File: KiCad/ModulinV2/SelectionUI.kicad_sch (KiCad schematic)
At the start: 24 parts, among them IC44 E-ULN2003D1013TR, IC45 E-ULN2003D1013TR, IC46 CD4028BM96, IC47 CD4028BM96

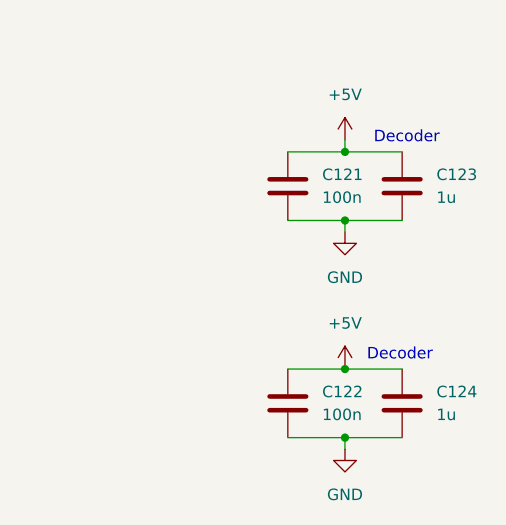
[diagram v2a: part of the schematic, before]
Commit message: Added footprints to all capacitors and potentiometers
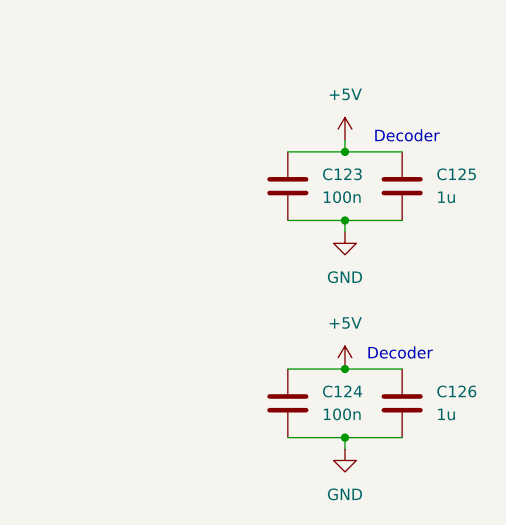
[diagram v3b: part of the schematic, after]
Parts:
- C123: renamed from C121; footprint SamacSys_Parts:CAPC1608X90N -> Capacitor_SMD:C_0603_1608Metric_Pad1.08x0.95mm_HandSolder
- C124: renamed from C122; footprint SamacSys_Parts:CAPC1608X90N -> Capacitor_SMD:C_0603_1608Metric_Pad1.08x0.95mm_HandSolder
- C125: renamed from C123; footprint SamacSys_Parts:CAPC1608X95N -> Capacitor_SMD:C_0603_1608Metric_Pad1.08x0.95mm_HandSolder
- C126: renamed from C124; footprint SamacSys_Parts:CAPC1608X95N -> Capacitor_SMD:C_0603_1608Metric_Pad1.08x0.95mm_HandSolder
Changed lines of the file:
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@@
 		(dnp no)
 		(fields_autoplaced yes)
-		(property "Reference" "#PWR0299"
+		(property "Reference" "#PWR0301"
 			(at 265.43 163.83 0)
 			(effects
@@
 			(project "ModulinV2"
 				(path "/c6b34a57-3941-4b56-8b80-1848c7f41082/ba5ade70-a939-4914-9429-1ad400c74d73/e799dfb0-018d-4a0c-90e3-bc5a892eb818"
-					(reference "#PWR0299")
+					(reference "#PWR0301")
 					(unit 1)
 				)
@@
 		(dnp no)
 		(fields_autoplaced yes)
-		(property "Reference" "#PWR0290"
+		(property "Reference" "#PWR0292"
 			(at 140.97 88.9 0)
 			(effects
@@
 			(project "ModulinV2"
 				(path "/c6b34a57-3941-4b56-8b80-1848c7f41082/ba5ade70-a939-4914-9429-1ad400c74d73/e799dfb0-018d-4a0c-90e3-bc5a892eb818"
-					(reference "#PWR0290")
+					(reference "#PWR0292")
 					(unit 1)
 				)
@@
 		(dnp no)
 		(fields_autoplaced yes)
-		(property "Reference" "#PWR0292"
+		(property "Reference" "#PWR0294"
 			(at 198.12 97.79 0)
 			(effects
@@
 			(project "ModulinV2"
 				(path "/c6b34a57-3941-4b56-8b80-1848c7f41082/ba5ade70-a939-4914-9429-1ad400c74d73/e799dfb0-018d-4a0c-90e3-bc5a892eb818"
-					(reference "#PWR0292")
+					(reference "#PWR0294")
 					(unit 1)
 				)
@@
 		(dnp no)
 		(fields_autoplaced yes)
-		(property "Reference" "#PWR0289"
+		(property "Reference" "#PWR0291"
 			(at 140.97 50.8 0)
 			(effects
@@
 			(project ""
 				(path "/c6b34a57-3941-4b56-8b80-1848c7f41082/ba5ade70-a939-4914-9429-1ad400c74d73/e799dfb0-018d-4a0c-90e3-bc5a892eb818"
-					(reference "#PWR0289")
+					(reference "#PWR0291")
 					(unit 1)
 				)
@@
 		(dnp no)
 		(fields_autoplaced yes)
-		(property "Reference" "#PWR0287"
+		(property "Reference" "#PWR0289"
 			(at 17.78 26.67 0)
 			(effects
@@
 			(project ""
 				(path "/c6b34a57-3941-4b56-8b80-1848c7f41082/ba5ade70-a939-4914-9429-1ad400c74d73/e799dfb0-018d-4a0c-90e3-bc5a892eb818"
-					(reference "#PWR0287")
+					(reference "#PWR0289")
 					(unit 1)
 				)
@@
 		(dnp no)
 		(fields_autoplaced yes)
-		(property "Reference" "#PWR0288"
+		(property "Reference" "#PWR0290"
 			(at 17.78 95.25 0)
 			(effects
@@
 			(project "ModulinV2"
 				(path "/c6b34a57-3941-4b56-8b80-1848c7f41082/ba5ade70-a939-4914-9429-1ad400c74d73/e799dfb0-018d-4a0c-90e3-bc5a892eb818"
-					(reference "#PWR0288")
+					(reference "#PWR0290")
 					(unit 1)
 				)
@@
 		(dnp no)
 		(fields_autoplaced yes)
-		(property "Reference" "#PWR0291"
+		(property "Reference" "#PWR0293"
 			(at 198.12 53.34 0)
 			(effects
@@
 			(project "ModulinV2"
 				(path "/c6b34a57-3941-4b56-8b80-1848c7f41082/ba5ade70-a939-4914-9429-1ad400c74d73/e799dfb0-018d-4a0c-90e3-bc5a892eb818"
-					(reference "#PWR0291")
+					(reference "#PWR0293")
 					(unit 1)
 				)
@@
 		(dnp no)
 		(fields_autoplaced yes)
-		(property "Reference" "C121"
+		(property "Reference" "C123"
 			(at 262.89 126.9999 0)
 			(effects
@@
 			)
 		)
-		(property "Footprint" "SamacSys_Parts:CAPC1608X90N"
+		(property "Footprint" "Capacitor_SMD:C_0603_1608Metric_Pad1.08x0.95mm_HandSolder"
 			(at 258.1148 124.46 0)
 			(effects
@@
 			(project "ModulinV2"
 				(path "/c6b34a57-3941-4b56-8b80-1848c7f41082/ba5ade70-a939-4914-9429-1ad400c74d73/e799dfb0-018d-4a0c-90e3-bc5a892eb818"
-					(reference "C121")
+					(reference "C123")
 					(unit 1)
 				)
@@
 		(dnp no)
 		(fields_autoplaced yes)
-		(property "Reference" "#PWR0296"
+		(property "Reference" "#PWR0298"
 			(at 265.43 127 0)
 			(effects
@@
 			(project "ModulinV2"
 				(path "/c6b34a57-3941-4b56-8b80-1848c7f41082/ba5ade70-a939-4914-9429-1ad400c74d73/e799dfb0-018d-4a0c-90e3-bc5a892eb818"
-					(reference "#PWR0296")
+					(reference "#PWR0298")
 					(unit 1)
 				)
@@
 		(dnp no)
 		(fields_autoplaced yes)
-		(property "Reference" "C123"
+		(property "Reference" "C125"
 			(at 275.59 126.9999 0)
 			(effects
@@
 			)
 		)
-		(property "Footprint" "SamacSys_Parts:CAPC1608X95N"
+		(property "Footprint" "Capacitor_SMD:C_0603_1608Metric_Pad1.08x0.95mm_HandSolder"
 			(at 270.8148 124.46 0)
 			(effects
@@
 			(project "ModulinV2"
 				(path "/c6b34a57-3941-4b56-8b80-1848c7f41082/ba5ade70-a939-4914-9429-1ad400c74d73/e799dfb0-018d-4a0c-90e3-bc5a892eb818"
-					(reference "C123")
+					(reference "C125")
 					(unit 1)
 				)
@@
 		(dnp no)
 		(fields_autoplaced yes)
-		(property "Reference" "#PWR0294"
+		(property "Reference" "#PWR0296"
 			(at 223.52 72.39 0)
 			(effects
@@
 			(project "ModulinV2"
 				(path "/c6b34a57-3941-4b56-8b80-1848c7f41082/ba5ade70-a939-4914-9429-1ad400c74d73/e799dfb0-018d-4a0c-90e3-bc5a892eb818"
-					(reference "#PWR0294")
+					(reference "#PWR0296")
 					(unit 1)
 				)
@@
 		(dnp no)
 		(fields_autoplaced yes)
-		(property "Reference" "#PWR0293"
+		(property "Reference" "#PWR0295"
 			(at 223.52 27.94 0)
 			(effects
@@
 			(project "ModulinV2"
 				(path "/c6b34a57-3941-4b56-8b80-1848c7f41082/ba5ade70-a939-4914-9429-1ad400c74d73/e799dfb0-018d-4a0c-90e3-bc5a892eb818"
-					(reference "#PWR0293")
+					(reference "#PWR0295")
 					(unit 1)
 				)
@@
 		(dnp no)
 		(fields_autoplaced yes)
-		(property "Reference" "C122"
+		(property "Reference" "C124"
 			(at 262.89 151.1299 0)
 			(effects
@@
 			)
 		)
-		(property "Footprint" "SamacSys_Parts:CAPC1608X90N"
+		(property "Footprint" "Capacitor_SMD:C_0603_1608Metric_Pad1.08x0.95mm_HandSolder"
 			(at 258.1148 148.59 0)
 			(effects
@@
 			(project "ModulinV2"
 				(path "/c6b34a57-3941-4b56-8b80-1848c7f41082/ba5ade70-a939-4914-9429-1ad400c74d73/e799dfb0-018d-4a0c-90e3-bc5a892eb818"
-					(reference "C122")
+					(reference "C124")
 					(unit 1)
 				)
@@
 		(dnp no)
 		(fields_autoplaced yes)
-		(property "Reference" "#PWR0295"
+		(property "Reference" "#PWR0297"
 			(at 233.68 90.17 0)
 			(effects
@@
 			(project "ModulinV2"
 				(path "/c6b34a57-3941-4b56-8b80-1848c7f41082/ba5ade70-a939-4914-9429-1ad400c74d73/e799dfb0-018d-4a0c-90e3-bc5a892eb818"
-					(reference "#PWR0295")
+					(reference "#PWR0297")
 					(unit 1)
 				)
@@
 		(dnp no)
 		(fields_autoplaced yes)
-		(property "Reference" "#PWR0297"
+		(property "Reference" "#PWR0299"
 			(at 265.43 139.7 0)
 			(effects
@@
 			(project "ModulinV2"
 				(path "/c6b34a57-3941-4b56-8b80-1848c7f41082/ba5ade70-a939-4914-9429-1ad400c74d73/e799dfb0-018d-4a0c-90e3-bc5a892eb818"
-					(reference "#PWR0297")
+					(reference "#PWR0299")
 					(unit 1)
 				)
@@
 		(dnp no)
 		(fields_autoplaced yes)
-		(property "Reference" "#PWR0298"
+		(property "Reference" "#PWR0300"
 			(at 265.43 152.4 0)
 			(effects
@@
 			(project "ModulinV2"
 				(path "/c6b34a57-3941-4b56-8b80-1848c7f41082/ba5ade70-a939-4914-9429-1ad400c74d73/e799dfb0-018d-4a0c-90e3-bc5a892eb818"
-					(reference "#PWR0298")
+					(reference "#PWR0300")
 					(unit 1)
 				)
@@
 		(dnp no)
 		(fields_autoplaced yes)
-		(property "Reference" "C124"
+		(property "Reference" "C126"
 			(at 275.59 151.1299 0)
 			(effects
@@
 			)
 		)
-		(property "Footprint" "SamacSys_Parts:CAPC1608X95N"
+		(property "Footprint" "Capacitor_SMD:C_0603_1608Metric_Pad1.08x0.95mm_HandSolder"
 			(at 270.8148 148.59 0)
 			(effects
@@
 			(project "ModulinV2"
 				(path "/c6b34a57-3941-4b56-8b80-1848c7f41082/ba5ade70-a939-4914-9429-1ad400c74d73/e799dfb0-018d-4a0c-90e3-bc5a892eb818"
-					(reference "C124")
+					(reference "C126")
 					(unit 1)
 				)

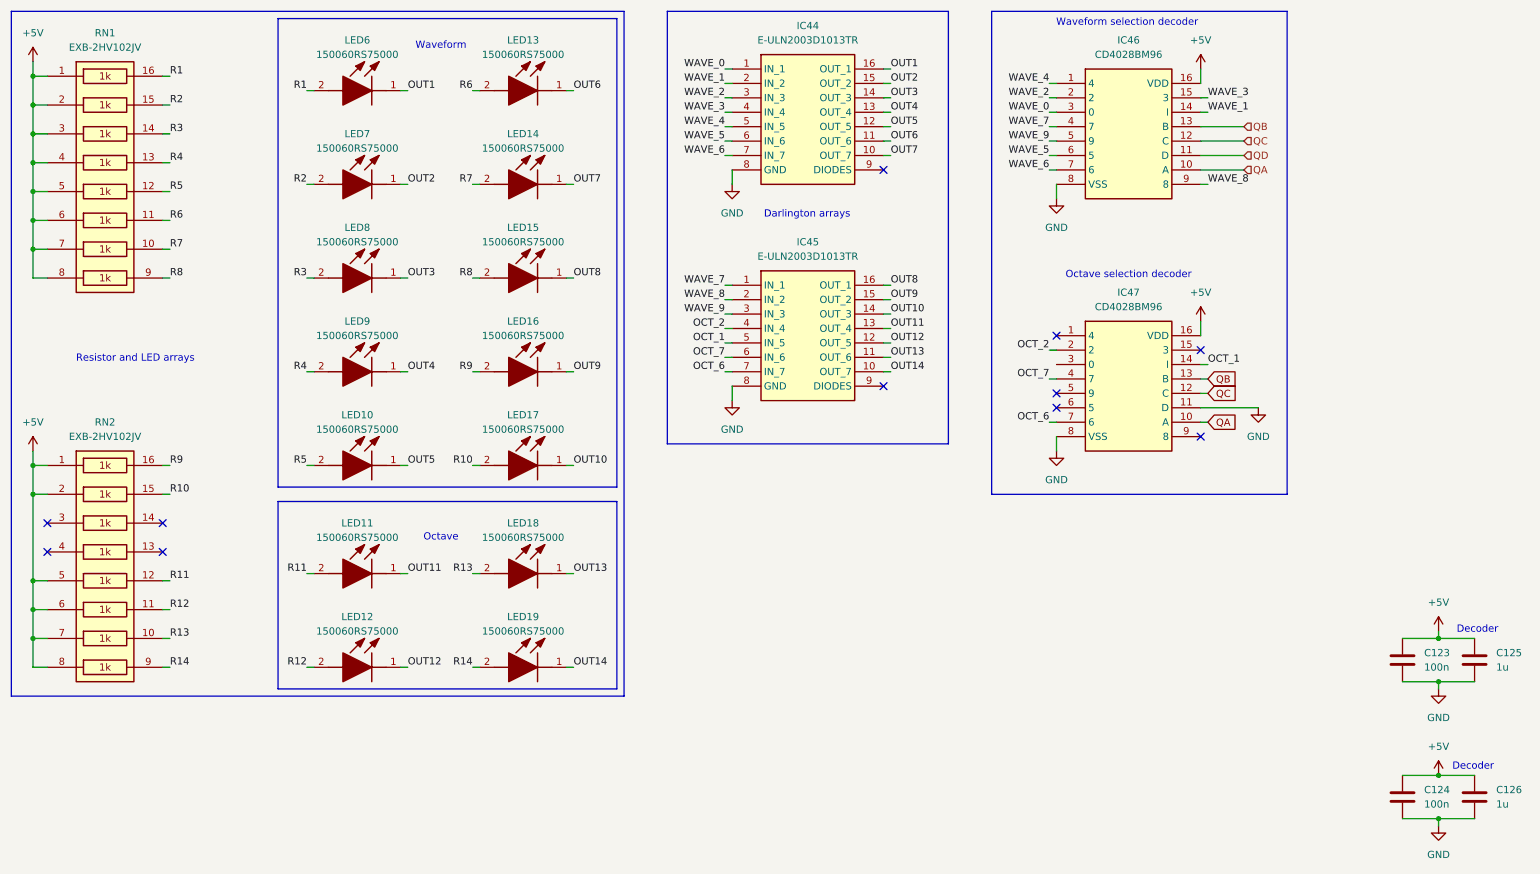
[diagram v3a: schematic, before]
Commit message: Finished Schematic, started on PCB
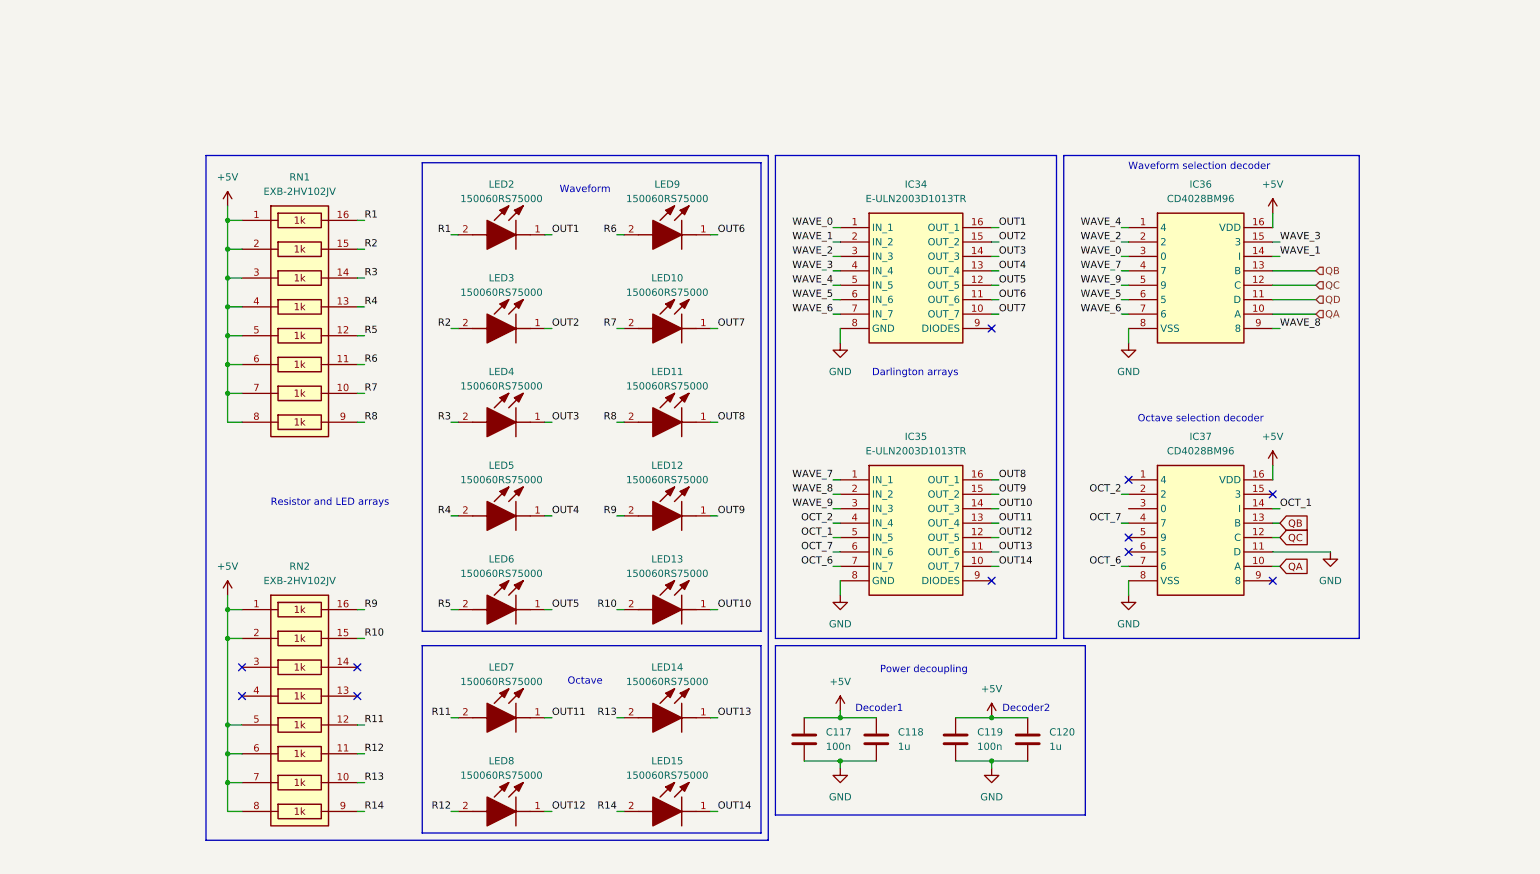
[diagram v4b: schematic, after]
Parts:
- renumbered C123 to C117, C125 to C118, C124 to C119, C126 to C120, IC44 to IC34, IC45 to IC35, IC46 to IC36, IC47 to IC37, LED14 to LED10, LED15 to LED11, LED16 to LED12, LED17 to LED13, LED18 to LED14, LED19 to LED15, LED6 to LED2, LED7 to LED3, LED8 to LED4, LED9 to LED5, LED10 to LED6, LED11 to LED7, LED12 to LED8, LED13 to LED9
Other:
- note added: "Decoder1"
- note added: "Decoder2"
- note added: "Power decoupling"
- note removed: "Decoder"
- moved on the sheet: C117, C118, C119, C120, IC34, IC35, IC36, IC37, LED10, LED11, LED12, LED13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

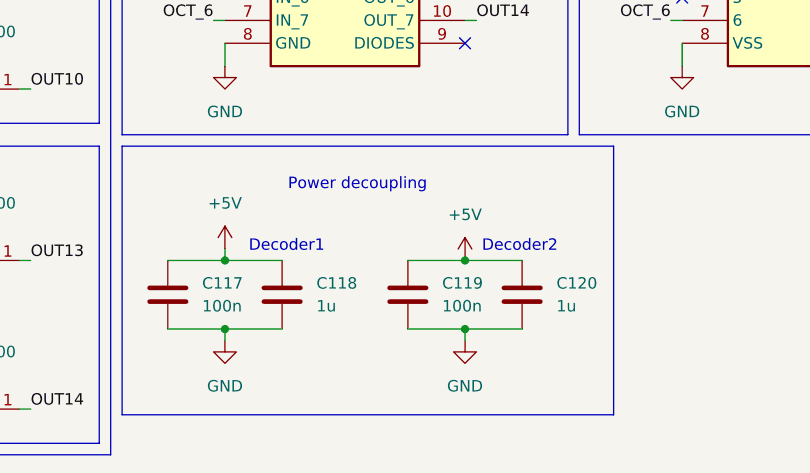
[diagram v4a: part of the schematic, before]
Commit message: Layed out Interface and PWR components and started with MCU layout
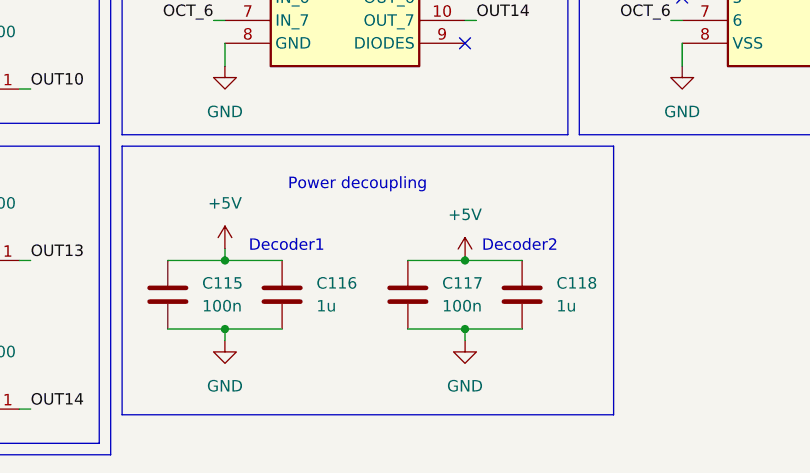
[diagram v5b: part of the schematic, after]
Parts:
- renumbered C117 to C115, C118 to C116, C119 to C117, C120 to C118
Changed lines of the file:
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@@
 		(dnp no)
 		(fields_autoplaced yes)
-		(property "Reference" "C117"
+		(property "Reference" "C115"
 			(at 157.48 140.9699 0)
 			(effects
@@
 			(project "ModulinV2"
 				(path "/c6b34a57-3941-4b56-8b80-1848c7f41082/ba5ade70-a939-4914-9429-1ad400c74d73/e799dfb0-018d-4a0c-90e3-bc5a892eb818"
-					(reference "C117")
+					(reference "C115")
 					(unit 1)
 				)
@@
 		(dnp no)
 		(fields_autoplaced yes)
-		(property "Reference" "C118"
+		(property "Reference" "C116"
 			(at 170.18 140.9699 0)
 			(effects
@@
 			(project "ModulinV2"
 				(path "/c6b34a57-3941-4b56-8b80-1848c7f41082/ba5ade70-a939-4914-9429-1ad400c74d73/e799dfb0-018d-4a0c-90e3-bc5a892eb818"
-					(reference "C118")
+					(reference "C116")
 					(unit 1)
 				)
@@
 		(dnp no)
 		(fields_autoplaced yes)
-		(property "Reference" "C119"
+		(property "Reference" "C117"
 			(at 184.15 140.9699 0)
 			(effects
@@
 			(project "ModulinV2"
 				(path "/c6b34a57-3941-4b56-8b80-1848c7f41082/ba5ade70-a939-4914-9429-1ad400c74d73/e799dfb0-018d-4a0c-90e3-bc5a892eb818"
-					(reference "C119")
+					(reference "C117")
 					(unit 1)
 				)
@@
 		(dnp no)
 		(fields_autoplaced yes)
-		(property "Reference" "C120"
+		(property "Reference" "C118"
 			(at 196.85 140.9699 0)
 			(effects
@@
 			(project "ModulinV2"
 				(path "/c6b34a57-3941-4b56-8b80-1848c7f41082/ba5ade70-a939-4914-9429-1ad400c74d73/e799dfb0-018d-4a0c-90e3-bc5a892eb818"
-					(reference "C120")
-					(unit 1)
-				)
+					(reference "C118")
+					(unit 1)
+				)
